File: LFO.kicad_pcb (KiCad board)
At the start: 2 copper layers, 39.6 x 100 mm, 0 parts

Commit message: Initial placement.
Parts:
- added C1: 22p, Capacitors_SMD:C_0603, B.Cu at (203.8, 124.1)
- added C10: 10u, Capacitors_SMD:CP_Elec_4x5.8, B.Cu at (244.1, 79.1)
- added C11: 100n, Capacitors_SMD:C_0603, B.Cu at (245.8, 76.1)
- added C12: 100n, Capacitors_SMD:C_0603, B.Cu at (248.9, 80.5)
- added C13: 10u, Capacitors_SMD:CP_Elec_4x5.8, B.Cu at (237.4, 79.1)
- added C14: 10u, Capacitors_SMD:CP_Elec_4x5.8, B.Cu at (248.5, 86.2)
- added C15: 100p, Capacitors_SMD:C_0603, B.Cu at (188.6, 93.0)
- added C16: 100p, Capacitors_SMD:C_0603, B.Cu at (198.2, 74.8)
- added C17: 47n, Capacitors_SMD:C_0603, B.Cu at (195.4, 73.4)
- added C18: 47n, Capacitors_SMD:C_0603, B.Cu at (201.1, 76.1)
- added C19: 47n, Capacitors_SMD:C_0603, B.Cu at (198.2, 73.4)
- added C2: 22p, Capacitors_SMD:C_0603, B.Cu at (203.8, 125.4)
- added C20: 47n, Capacitors_SMD:C_0603, B.Cu at (191.5, 94.4)
- added C21: 100p, Capacitors_SMD:C_0603, B.Cu at (195.4, 76.1)
- added C22: C, Capacitors_SMD:C_0603, B.Cu at (195.4, 74.8)
- added C23: 100n, Capacitors_SMD:C_0603, B.Cu at (188.6, 94.4)
- added C24: 100n, Capacitors_SMD:C_0603, B.Cu at (198.2, 76.1)
- added C25: 100n, Capacitors_SMD:C_0603, B.Cu at (214.8, 111.5)
- added C3: 100n, Capacitors_SMD:C_0603, B.Cu at (206.7, 125.4)
- added C4: 470p, Capacitors_SMD:C_0603, B.Cu at (139.1, 142.3)
- added C5: 100n, Capacitors_SMD:C_0603, B.Cu at (138.6, 68.9)
- added C6: 100n, Capacitors_SMD:C_0603, B.Cu at (135.3, 139.5)
- added C7: 470p, Capacitors_SMD:C_0603, B.Cu at (139.1, 128.9)
- added C8: 100n, Capacitors_SMD:C_0603, B.Cu at (138.6, 109.8)
- added C9: 100n, Capacitors_SMD:C_0603, B.Cu at (135.3, 126.1)
- added D1: LED, LEDs:LED_D3.0mm, F.Cu at (147.2, 126.6)
- added D2: LED, LEDs:LED_D3.0mm, F.Cu at (147.2, 139.3)
- added D3: DFLR1400-7, Diodes_SMD:D_PowerDI-123, B.Cu at (250.0, 82.5)
- added D4: LED, LEDs:LED_1206, B.Cu at (236.7, 75.7)
- added D5: DFLR1400-7, Diodes_SMD:D_PowerDI-123, B.Cu at (241.9, 75.4)
- added J1: AudioJack2_SwitchT, Local:PJ398SM, F.Cu at (138.3, 132.9)
- added J2: AudioJack2_SwitchT, Local:PJ398SM, F.Cu at (158.7, 120.2)
- added J3: AudioJack2_SwitchT, Local:PJ398SM, F.Cu at (138.3, 120.2)
- added J4: AudioJack2_SwitchT, Local:PJ398SM, F.Cu at (158.7, 132.9)
- added J5: AudioJack2_SwitchT, Local:PJ398SM, F.Cu at (138.3, 145.6)
- added J6: AudioJack2_SwitchT, Local:PJ398SM, F.Cu at (158.7, 145.6)
- added J7: Conn_02x03_Odd_Even, Pin_Headers:Pin_Header_Straight_2x03_Pitch2.54mm, B.Cu at (189.8, 116.7)
- added J8: Conn_02x05_Odd_Even, Pin_Headers:Pin_Header_Straight_2x05_Pitch2.54mm, B.Cu at (147.2, 69.4)
- added Q1: BC847, TO_SOT_Packages_SMD:SOT-23, B.Cu at (138.1, 148.4)
- added R1: 10k, Resistors_SMD:R_0603, B.Cu at (203.7, 122.6)
- added R10: 200k, Resistors_SMD:R_0603, B.Cu at (142.9, 139.5)
- added R11: 47k, Resistors_SMD:R_0603, B.Cu at (142.9, 136.8)
- added R12: 100k, Resistors_SMD:R_0603, B.Cu at (135.3, 128.9)
- added R13: 200k, Resistors_SMD:R_0603, B.Cu at (142.9, 128.9)
- added R14: 100k, Resistors_SMD:R_0603, B.Cu at (139.1, 126.1)
- added R15: 100k, Resistors_SMD:R_0603, B.Cu at (142.9, 126.1)
- added R16: 47k, Resistors_SMD:R_0603, B.Cu at (142.9, 123.3)
- added R17: 330, Resistors_SMD:R_0603, B.Cu at (248.8, 79.0)
- added R18: 68k, Resistors_SMD:R_0603, B.Cu at (188.5, 87.2)
- added R19: 68k, Resistors_SMD:R_0603, B.Cu at (211.4, 76.1)
- added R2: 330, Resistors_SMD:R_0603, B.Cu at (198.8, 120.8)
- added R20: 470, Resistors_SMD:R_0603, B.Cu at (191.0, 90.0)
- added R21: 470, Resistors_SMD:R_0603, B.Cu at (208.6, 74.6)
- added R22: 470, Resistors_SMD:R_0603, B.Cu at (191.0, 91.5)
- added R23: 470, Resistors_SMD:R_0603, B.Cu at (200.9, 74.7)
- added R24: 33k, Resistors_SMD:R_0603, B.Cu at (208.9, 76.1)
- added R25: 68k, Resistors_SMD:R_0603, B.Cu at (191.3, 93.0)
- added R26: 1k, Resistors_SMD:R_0603, B.Cu at (203.5, 74.6)
- added R27: 100k, Resistors_SMD:R_0603, B.Cu at (200.9, 73.2)
- added R28: 33k, Resistors_SMD:R_0603, B.Cu at (203.8, 76.1)
- added R29: 20k, Resistors_SMD:R_0603, B.Cu at (188.5, 91.6)
- added R3: 10k, Resistors_SMD:R_0603, B.Cu at (141.1, 148.0)
- added R30: 10k, Resistors_SMD:R_0603, B.Cu at (188.5, 90.1)
- added R31: 68k, Resistors_SMD:R_0603, B.Cu at (206.3, 76.1)
- added R32: 68k, Resistors_SMD:R_0603, B.Cu at (188.5, 88.7)
- added R33: 68k, Resistors_SMD:R_0603, B.Cu at (206.0, 74.6)
- added R34: 1k, Resistors_SMD:R_0603, B.Cu at (211.1, 74.6)
- added R35: 100k, Resistors_SMD:R_0603, B.Cu at (188.5, 85.7)
- added R36: 33k, Resistors_SMD:R_0603, B.Cu at (191.0, 88.5)
- added R37: 68k, Resistors_SMD:R_0603, B.Cu at (214.0, 76.1)
- added R38: 4k7, Resistors_SMD:R_0603, B.Cu at (222.6, 111.4)
- added R39: 15k, Resistors_SMD:R_0603, B.Cu at (227.6, 111.4)
- added R4: 100k, Resistors_SMD:R_0603, B.Cu at (141.1, 149.5)
- added R40: 68k, Resistors_SMD:R_0603, B.Cu at (220.0, 111.4)
- added R41: 33k, Resistors_SMD:R_0603, B.Cu at (227.6, 112.9)
- added R42: 3k3, Resistors_SMD:R_0603, B.Cu at (217.5, 111.4)
- added R43: 22k, Resistors_SMD:R_0603, B.Cu at (225.1, 111.4)
- added R5: 1k, Resistors_SMD:R_0603, B.Cu at (159.8, 144.8)
- added R6: 330, Resistors_SMD:R_0603, B.Cu at (157.3, 144.8)
- added R7: 100k, Resistors_SMD:R_0603, B.Cu at (135.3, 142.3)
- added R8: 200k, Resistors_SMD:R_0603, B.Cu at (142.9, 142.3)
- added R9: 100k, Resistors_SMD:R_0603, B.Cu at (139.1, 139.5)
- added RV1: 100k, Local:AlpsRK09K, F.Cu at (138.4, 64.3)
- added RV2: 100k, Local:AlpsRK09K, F.Cu at (138.3, 105.0)
- added RV3: 100k, Local:AlpsRK09K, F.Cu at (138.3, 84.7)
- added RV4: 100k, Local:AlpsRK09K, F.Cu at (158.7, 84.7)
- added SW1: SW_Push, Buttons_Switches_THT:SW_PUSH_6mm_h9.5mm, F.Cu at (145.2, 111.6)
- added SW2: SW_SPDT_MSM, Local:SPDT, F.Cu at (158.7, 64.4)
- added SW3: SW_SPDT_MSM, Local:SPDT, F.Cu at (158.7, 105.0)
- added U1: ATtiny84-20MU, Housings_DFN_QFN:QFN-20-1EP_4x4mm_Pitch0.5mm, B.Cu at (190.6, 107.2)
- added U2: 74AHCT1G125, TO_SOT_Packages_SMD:SOT-23-5, B.Cu at (157.9, 147.4)
- added U3: MCP6002-xMS, Housings_SSOP:MSOP-8_3x3mm_Pitch0.65mm, B.Cu at (139.1, 134.2)
- added U4: MCP6002-xMS, Housings_SSOP:MSOP-8_3x3mm_Pitch0.65mm, B.Cu at (139.1, 120.7)
- added U5: L7805, TO_SOT_Packages_SMD:TO-252-3_TabPin2, B.Cu at (239.6, 85.1)
- added U6: LM324, Housings_DFN_QFN:QFN-16-1EP_3x3mm_Pitch0.5mm, B.Cu at (191.8, 74.7)
- added Y1: 20MHz, Crystals:Crystal_SMD_Abracon_ABM3-2pin_5.0x3.2mm, B.Cu at (197.5, 116.6)

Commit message: Updated footprint library.
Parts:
- C1, C11, C12, C15, C16, C17, C18, C19, C2, C20, C21, C23, C24, C25, C3, C4, C5, C6, C7, C8, C9: footprint Capacitors_SMD:C_0603 -> Capacitor_SMD:C_0603_1608Metric
- C10, C13, C14: footprint Capacitors_SMD:CP_Elec_4x5.8 -> Capacitor_SMD:CP_Elec_4x5.8
- C22: value C -> 100n; footprint Capacitors_SMD:C_0603 -> Capacitor_SMD:C_0603_1608Metric
- D1, D2: footprint LEDs:LED_D3.0mm -> LED_THT:LED_D3.0mm
- D3, D5: footprint Diodes_SMD:D_PowerDI-123 -> Diode_SMD:D_PowerDI-123
- D4: footprint LEDs:LED_1206 -> LED_SMD:LED_1206_3216Metric_Castellated
- J7: footprint Pin_Headers:Pin_Header_Straight_2x03_Pitch2.54mm -> Connector_PinHeader_2.54mm:PinHeader_2x03_P2.54mm_Vertical
- J8: footprint Pin_Headers:Pin_Header_Straight_2x05_Pitch2.54mm -> Connector_PinHeader_2.54mm:PinHeader_2x05_P2.54mm_Vertical
- Q1: footprint TO_SOT_Packages_SMD:SOT-23 -> Package_TO_SOT_SMD:SOT-23
- R1, R10, R11, R12, R13, R14, R15, R16, R17, R18, R19, R2, R20, R21, R22, R23, R24, R25, R26, R27, R28, R29, R3, R30, R31, R32, R33, R34, R35, R36, R37, R38, R39, R4, R40, R41, R42, R43, R5, R6, R7, R8, R9: footprint Resistors_SMD:R_0603 -> Resistor_SMD:R_0603_1608Metric
- SW1: footprint Buttons_Switches_THT:SW_PUSH_6mm_h9.5mm -> Button_Switch_THT:SW_PUSH_6mm_H9.5mm
- U1: footprint Housings_DFN_QFN:QFN-20-1EP_4x4mm_Pitch0.5mm -> Package_DFN_QFN:QFN-20-1EP_4x4mm_P0.5mm_EP2.5x2.5mm
- U2: footprint TO_SOT_Packages_SMD:SOT-23-5 -> Package_TO_SOT_SMD:SOT-23-5
- U3, U4: footprint Housings_SSOP:MSOP-8_3x3mm_Pitch0.65mm -> Package_SO:MSOP-8_3x3mm_P0.65mm
- U5: footprint TO_SOT_Packages_SMD:TO-252-3_TabPin2 -> Package_TO_SOT_SMD:TO-252-3_TabPin2
- U6: footprint Housings_DFN_QFN:QFN-16-1EP_3x3mm_Pitch0.5mm -> Package_DFN_QFN:QFN-16-1EP_3x3mm_P0.5mm_EP1.8x1.8mm
- Y1: footprint Crystals:Crystal_SMD_Abracon_ABM3-2pin_5.0x3.2mm -> Crystal:Crystal_SMD_Abracon_ABM3-2Pin_5.0x3.2mm

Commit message: First complete placement.
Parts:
- added D6: LM4040DBZ-10, Package_TO_SOT_SMD:SOT-23, B.Cu at (157.9, 141.6)
- added R44: 2k2, Resistor_SMD:R_0603_1608Metric, B.Cu at (158.7, 137.0)
- moved C10 110.9 mm to (133.3, 77.1), turned to 270 degrees
- moved C14 109.1 mm to (139.9, 77.1), turned to 270 degrees
- moved D4 99.4 mm to (138.3, 61.3), turned to 90 degrees
- moved D3 98.8 mm to (153.8, 60.0), turned to 90 degrees
- moved C12 97.0 mm to (152.1, 75.0), turned to 180 degrees
- moved C11 93.8 mm to (152.1, 79.6), turned to 180 degrees
- moved C13 90.9 mm to (146.5, 77.1), turned to 270 degrees
- moved D5 88.3 mm to (153.8, 68.7), turned to 90 degrees
- moved R17 88.0 mm to (163.2, 58.5)
- moved R34 81.1 mm to (163.2, 140.1)
- moved U5 79.8 mm to (160.2, 77.3)
- moved R38 77.7 mm to (163.2, 61.3)
- moved R39 73.3 mm to (154.8, 102.5), turned to 270 degrees
- moved R31 73.3 mm to (158.7, 131.7)
- moved R41 73.0 mm to (154.8, 106.3), turned to 270 degrees
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
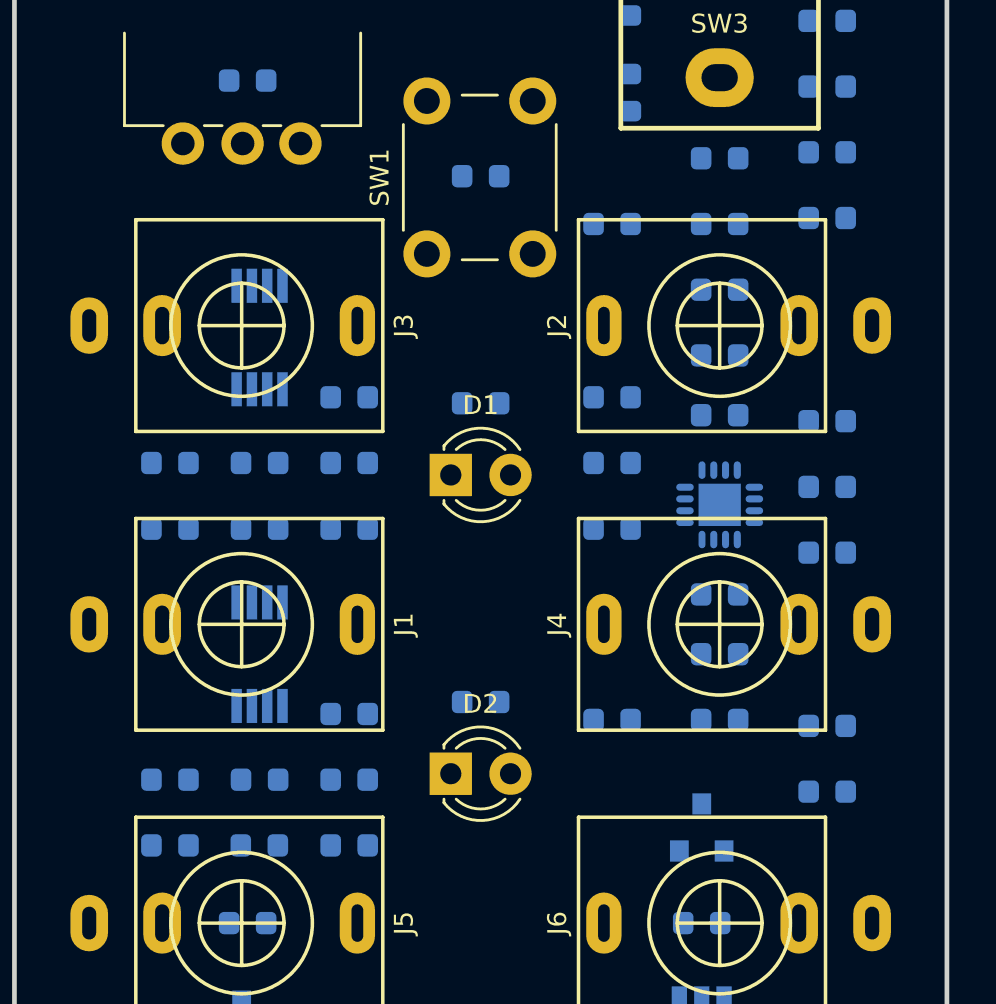
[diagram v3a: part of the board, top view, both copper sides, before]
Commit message: Better orientation of op-amp.
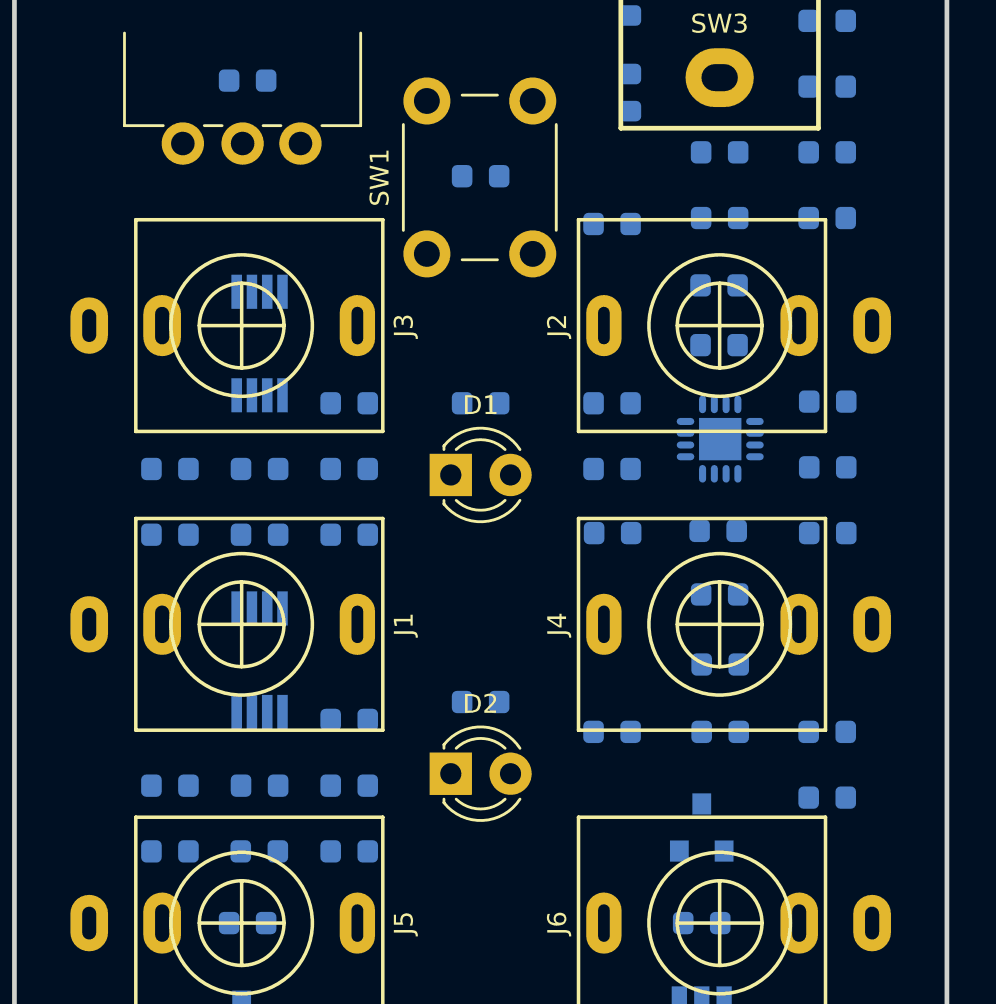
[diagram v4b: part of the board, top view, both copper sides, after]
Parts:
- moved R33 15.9 mm to (158.7, 134.6), turned to 0 degrees
- moved R29 10.8 mm to (163.3, 129.1)
- moved C15 10.6 mm to (163.3, 123.5), turned to 180 degrees
- moved R27 10.3 mm to (154.1, 129.1), turned to 180 degrees
- moved C24 9.81 mm to (154.1, 123.5), turned to 0 degrees
- moved R36 9.81 mm to (154.1, 126.3), turned to 0 degrees
- moved R18 9.17 mm to (163.3, 126.3), turned to 180 degrees
- moved C16 2.98 mm to (158.6, 118.5)
- moved R19 2.98 mm to (158.6, 121.1)
- moved U6 2.79 mm to (158.7, 125.1), turned to 180 degrees
- moved R31 2.70 mm to (158.6, 129.0)
- moved C21 2.54 mm to (158.7, 131.7)
- moved R44 0.51 mm to (158.7, 137.5), turned to 0 degrees
- moved R30 0.51 mm to (154.1, 137.5)
- moved C4 0.25 mm to (139.1, 142.6)
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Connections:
- U6 pad 12: Net-(R36-Pad2) -> Net-(R28-Pad2)
- U6 pad 13: Net-(C16-Pad1) -> Net-(C16-Pad2)
- U6 pad 14: Net-(C21-Pad1) -> Net-(C16-Pad1)
- U6 pad 5: Net-(R28-Pad2) -> Net-(R36-Pad2)
- U6 pad 6: Net-(C16-Pad2) -> Net-(C16-Pad1)
- U6 pad 7: Net-(C16-Pad1) -> Net-(C21-Pad1)

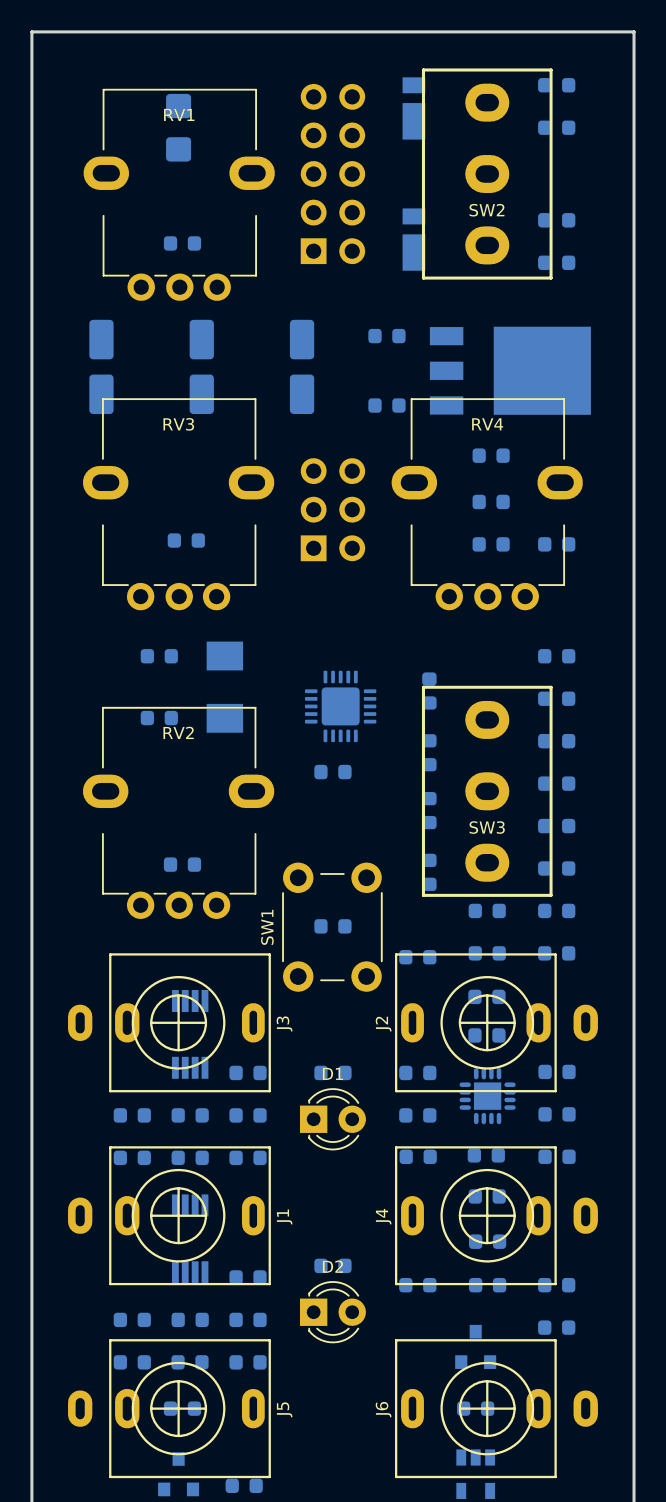
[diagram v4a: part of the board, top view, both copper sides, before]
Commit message: Manually routed power.
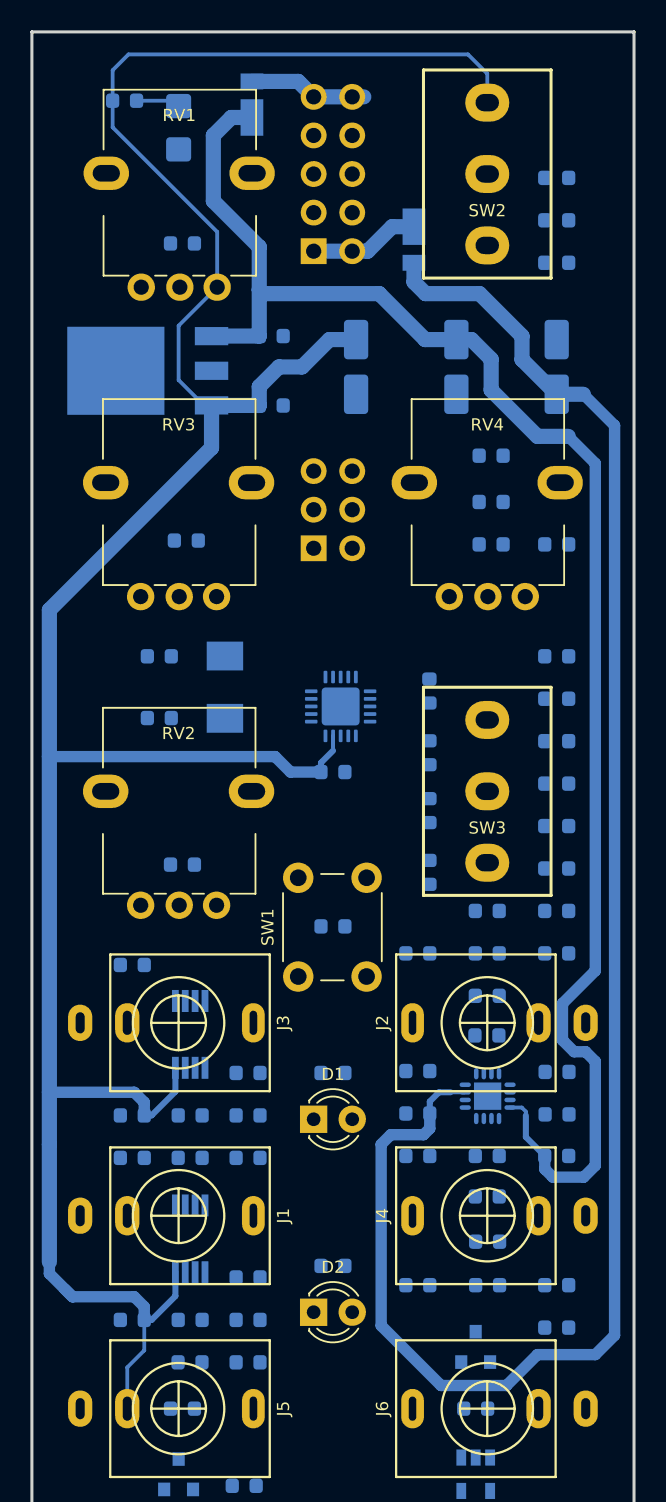
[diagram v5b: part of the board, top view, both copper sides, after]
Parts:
- moved R17 28.5 mm to (134.8, 59.5)
- moved U5 23.9 mm to (136.3, 77.3), turned to 180 degrees
- moved C10 23.4 mm to (156.6, 77.1)
- moved C14 23.4 mm to (163.2, 77.1)
- moved R29 14.2 mm to (158.7, 115.7)
- moved C23 14.1 mm to (163.2, 129.0)
- moved R7 13.5 mm to (135.3, 129.1), turned to 180 degrees
- moved R12 12.7 mm to (135.3, 116.4), turned to 180 degrees
- moved D3 10.7 mm to (143.2, 59.8)
- moved C11 8.89 mm to (144.4, 75.0), turned to 0 degrees
- moved C12 8.89 mm to (144.4, 79.6), turned to 0 degrees
- moved R27 5.65 mm to (154.1, 123.4)
- moved R36 5.29 mm to (158.7, 129.0)
- moved R31 4.51 mm to (154.1, 129.0)
- moved C13 3.56 mm to (150.0, 77.1)
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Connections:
- U1 pad 2: TRIG -> SYNC
- U1 pad 3: SYNC -> TRIG
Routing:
- net +5V: track 0.00 -> 181.5 mm
- net -12V: track 0.00 -> 117.5 mm
- net +12V: track 0.00 -> 106.5 mm
- net Net-(D3-Pad2): track 0.00 -> 7.79 mm
- net Net-(D5-Pad1): track 0.00 -> 7.27 mm
- net Net-(D4-Pad2): track 0.00 -> 2.91 mm
